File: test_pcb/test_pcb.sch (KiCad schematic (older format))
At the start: 88 parts, among them K0 KEYSW, K1 KEYSW, K10 KEYSW, K12 KEYSW, K13 KEYSW, K14 KEYSW, K15 KEYSW, K16 KEYSW, K17 KEYSW, K18 KEYSW, K2 KEYSW, K20 KEYSW, K21 KEYSW, K22 KEYSW, K3 KEYSW, K4 KEYSW, K5 KEYSW, K6 KEYSW, K7 KEYSW, K8 KEYSW, K9 KEYSW, P1 CONN_01X15, P10 CONN_01X01, P11 CONN_01X01, P12 CONN_01X01, P13 CONN_01X01, P14 CONN_01X01, P15 CONN_01X01, P2 CONN_01X08, P3 CONN_01X06, P4 CONN_01X01, P5 CONN_01X01, P6 CONN_01X01, P7 CONN_01X01, P8 CONN_01X01, P9 CONN_01X01, U1 STP16CP05

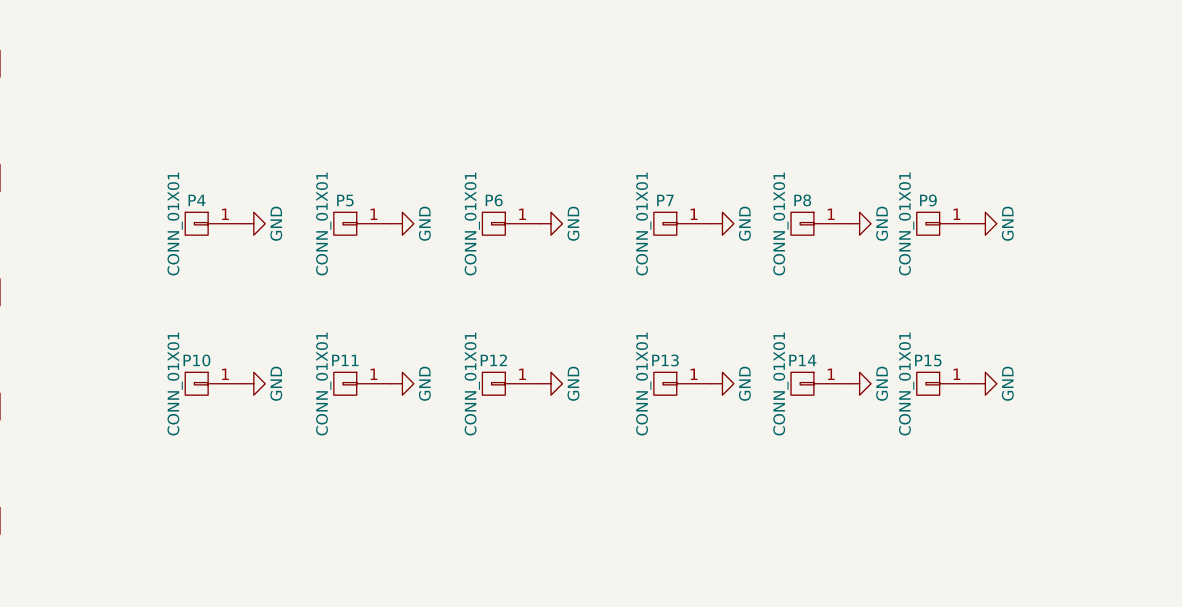
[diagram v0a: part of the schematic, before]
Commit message: test groundplane loop eliminiation, they are sneeky
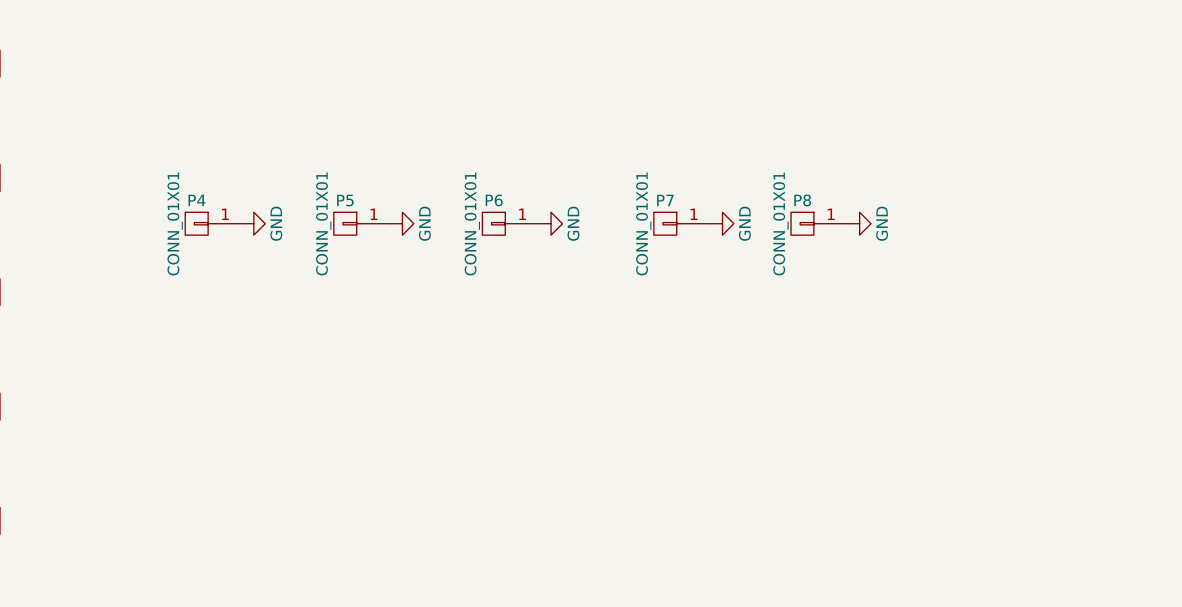
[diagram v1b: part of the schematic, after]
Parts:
- removed P10, P11, P12, P13, P14, P15, P9: CONN_01X01, Socket_Strips:Socket_Strip_Straight_1x01_Pitch1.27mm, symbol CONN_01X01
- P4, P5, P6, P7, P8: footprint Socket_Strips:Socket_Strip_Straight_1x01_Pitch1.27mm -> cherry_rgb:VIA127
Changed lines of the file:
@@
-$EndComp
-$Comp
-L GND #PWR016
-U 1 1 58BB11EE
-P 8100 5750
-F 0 "#PWR016" H 8100 5500 50  0001 C CNN
-F 1 "GND" H 8100 5600 50  0000 C CNN
-F 2 "" H 8100 5750 50  0000 C CNN
-F 3 "" H 8100 5750 50  0000 C CNN
-	1    8100 5750
-	0    -1   1    0
-$EndComp
-$Comp
-L CONN_01X01 P14
-U 1 1 58BB11E8
-P 7900 5750
-F 0 "P14" H 7900 5850 50  0000 C CNN
-F 1 "CONN_01X01" V 8000 5750 50  0000 C CNN
-F 2 "Socket_Strips:Socket_Strip_Straight_1x01_Pitch1.27mm" H 7900 5750 50  0001 C CNN
-F 3 "" H 7900 5750 50  0000 C CNN
-	1    7900 5750
-	-1   0    0    -1
-$EndComp
-$Comp
-L GND #PWR015
-U 1 1 58BB11E2
-P 8650 5750
-F 0 "#PWR015" H 8650 5500 50  0001 C CNN
-F 1 "GND" H 8650 5600 50  0000 C CNN
-F 2 "" H 8650 5750 50  0000 C CNN
-F 3 "" H 8650 5750 50  0000 C CNN
-	1    8650 5750
-	0    -1   1    0
-$EndComp
-$Comp
-L CONN_01X01 P15
-U 1 1 58BB11DC
-P 8450 5750
-F 0 "P15" H 8450 5850 50  0000 C CNN
-F 1 "CONN_01X01" V 8550 5750 50  0000 C CNN
-F 2 "Socket_Strips:Socket_Strip_Straight_1x01_Pitch1.27mm" H 8450 5750 50  0001 C CNN
-F 3 "" H 8450 5750 50  0000 C CNN
-	1    8450 5750
-	-1   0    0    -1
-$EndComp
-$Comp
-L GND #PWR014
-U 1 1 58BB11D6
-P 6750 5750
-F 0 "#PWR014" H 6750 5500 50  0001 C CNN
-F 1 "GND" H 6750 5600 50  0000 C CNN
-F 2 "" H 6750 5750 50  0000 C CNN
-F 3 "" H 6750 5750 50  0000 C CNN
-	1    6750 5750
-	0    -1   1    0
-$EndComp
-$Comp
-L CONN_01X01 P12
-U 1 1 58BB11D0
-P 6550 5750
-F 0 "P12" H 6550 5850 50  0000 C CNN
-F 1 "CONN_01X01" V 6650 5750 50  0000 C CNN
-F 2 "Socket_Strips:Socket_Strip_Straight_1x01_Pitch1.27mm" H 6550 5750 50  0001 C CNN
-F 3 "" H 6550 5750 50  0000 C CNN
-	1    6550 5750
-	-1   0    0    -1
-$EndComp
-$Comp
-L GND #PWR013
-U 1 1 58BB11CA
-P 7500 5750
-F 0 "#PWR013" H 7500 5500 50  0001 C CNN
-F 1 "GND" H 7500 5600 50  0000 C CNN
-F 2 "" H 7500 5750 50  0000 C CNN
-F 3 "" H 7500 5750 50  0000 C CNN
-	1    7500 5750
-	0    -1   1    0
-$EndComp
-$Comp
-L CONN_01X01 P13
-U 1 1 58BB11C4
-P 7300 5750
-F 0 "P13" H 7300 5850 50  0000 C CNN
-F 1 "CONN_01X01" V 7400 5750 50  0000 C CNN
-F 2 "Socket_Strips:Socket_Strip_Straight_1x01_Pitch1.27mm" H 7300 5750 50  0001 C CNN
-F 3 "" H 7300 5750 50  0000 C CNN
-	1    7300 5750
-	-1   0    0    -1
 $EndComp
 $Comp
 L GND #PWR012
-U 1 1 58BB11BE
-P 6100 5750
-F 0 "#PWR012" H 6100 5500 50  0001 C CNN
-F 1 "GND" H 6100 5600 50  0000 C CNN
-F 2 "" H 6100 5750 50  0000 C CNN
-F 3 "" H 6100 5750 50  0000 C CNN
-	1    6100 5750
-	0    -1   1    0
-$EndComp
-$Comp
-L CONN_01X01 P11
-U 1 1 58BB11B8
-P 5900 5750
-F 0 "P11" H 5900 5850 50  0000 C CNN
-F 1 "CONN_01X01" V 6000 5750 50  0000 C CNN
-F 2 "Socket_Strips:Socket_Strip_Straight_1x01_Pitch1.27mm" H 5900 5750 50  0001 C CNN
-F 3 "" H 5900 5750 50  0000 C CNN
-	1    5900 5750
-	-1   0    0    -1
-$EndComp
-$Comp
-L GND #PWR011
-U 1 1 58BB11B2
-P 5450 5750
-F 0 "#PWR011" H 5450 5500 50  0001 C CNN
-F 1 "GND" H 5450 5600 50  0000 C CNN
-F 2 "" H 5450 5750 50  0000 C CNN
-F 3 "" H 5450 5750 50  0000 C CNN
-	1    5450 5750
-	0    -1   1    0
-$EndComp
-$Comp
-L CONN_01X01 P10
-U 1 1 58BB11AC
-P 5250 5750
-F 0 "P10" H 5250 5850 50  0000 C CNN
-F 1 "CONN_01X01" V 5350 5750 50  0000 C CNN
-F 2 "Socket_Strips:Socket_Strip_Straight_1x01_Pitch1.27mm" H 5250 5750 50  0001 C CNN
-F 3 "" H 5250 5750 50  0000 C CNN
-	1    5250 5750
-	-1   0    0    -1
-$EndComp
-$Comp
-L GND #PWR010
 U 1 1 58BAEE49
 P 8100 5050
-F 0 "#PWR010" H 8100 4800 50  0001 C CNN
+F 0 "#PWR012" H 8100 4800 50  0001 C CNN
 F 1 "GND" H 8100 4900 50  0000 C CNN
 F 2 "" H 8100 5050 50  0000 C CNN
@@
 F 0 "P8" H 7900 5150 50  0000 C CNN
 F 1 "CONN_01X01" V 8000 5050 50  0000 C CNN
-F 2 "Socket_Strips:Socket_Strip_Straight_1x01_Pitch1.27mm" H 7900 5050 50  0001 C CNN
+F 2 "cherry_rgb:VIA127" H 7900 5050 50  0001 C CNN
 F 3 "" H 7900 5050 50  0000 C CNN
 	1    7900 5050
@@
 $EndComp
 $Comp
-L GND #PWR09
-U 1 1 58BAEE3D
-P 8650 5050
-F 0 "#PWR09" H 8650 4800 50  0001 C CNN
-F 1 "GND" H 8650 4900 50  0000 C CNN
-F 2 "" H 8650 5050 50  0000 C CNN
-F 3 "" H 8650 5050 50  0000 C CNN
-	1    8650 5050
-	0    -1   1    0
-$EndComp
-$Comp
-L CONN_01X01 P9
-U 1 1 58BAEE37
-P 8450 5050
-F 0 "P9" H 8450 5150 50  0000 C CNN
-F 1 "CONN_01X01" V 8550 5050 50  0000 C CNN
-F 2 "Socket_Strips:Socket_Strip_Straight_1x01_Pitch1.27mm" H 8450 5050 50  0001 C CNN
-F 3 "" H 8450 5050 50  0000 C CNN
-	1    8450 5050
-	-1   0    0    -1
-$EndComp
-$Comp
-L GND #PWR08
+L GND #PWR014
 U 1 1 58BAEE31
 P 6750 5050
-F 0 "#PWR08" H 6750 4800 50  0001 C CNN
+F 0 "#PWR014" H 6750 4800 50  0001 C CNN
 F 1 "GND" H 6750 4900 50  0000 C CNN
 F 2 "" H 6750 5050 50  0000 C CNN
@@
 F 0 "P6" H 6550 5150 50  0000 C CNN
 F 1 "CONN_01X01" V 6650 5050 50  0000 C CNN
-F 2 "Socket_Strips:Socket_Strip_Straight_1x01_Pitch1.27mm" H 6550 5050 50  0001 C CNN
+F 2 "cherry_rgb:VIA127" H 6550 5050 50  0001 C CNN
 F 3 "" H 6550 5050 50  0000 C CNN
 	1    6550 5050
@@
 $EndComp
 $Comp
-L GND #PWR07
+L GND #PWR015
 U 1 1 58BAD6B9
 P 7500 5050
-F 0 "#PWR07" H 7500 4800 50  0001 C CNN
+F 0 "#PWR015" H 7500 4800 50  0001 C CNN
 F 1 "GND" H 7500 4900 50  0000 C CNN
 F 2 "" H 7500 5050 50  0000 C CNN
@@
 F 0 "P7" H 7300 5150 50  0000 C CNN
 F 1 "CONN_01X01" V 7400 5050 50  0000 C CNN
-F 2 "Socket_Strips:Socket_Strip_Straight_1x01_Pitch1.27mm" H 7300 5050 50  0001 C CNN
+F 2 "cherry_rgb:VIA127" H 7300 5050 50  0001 C CNN
 F 3 "" H 7300 5050 50  0000 C CNN
 	1    7300 5050
@@
 $EndComp
 $Comp
-L GND #PWR06
+L GND #PWR016
 U 1 1 58BACEDF
 P 6100 5050
-F 0 "#PWR06" H 6100 4800 50  0001 C CNN
+F 0 "#PWR016" H 6100 4800 50  0001 C CNN
 F 1 "GND" H 6100 4900 50  0000 C CNN
 F 2 "" H 6100 5050 50  0000 C CNN
@@
 F 0 "P5" H 5900 5150 50  0000 C CNN
 F 1 "CONN_01X01" V 6000 5050 50  0000 C CNN
-F 2 "Socket_Strips:Socket_Strip_Straight_1x01_Pitch1.27mm" H 5900 5050 50  0001 C CNN
+F 2 "cherry_rgb:VIA127" H 5900 5050 50  0001 C CNN
 F 3 "" H 5900 5050 50  0000 C CNN
 	1    5900 5050
@@
 $EndComp
 $Comp
-L GND #PWR05
+L GND #PWR017
 U 1 1 58BABD17
 P 5450 5050
-F 0 "#PWR05" H 5450 4800 50  0001 C CNN
+F 0 "#PWR017" H 5450 4800 50  0001 C CNN
 F 1 "GND" H 5450 4900 50  0000 C CNN
 F 2 "" H 5450 5050 50  0000 C CNN
@@
 F 0 "P4" H 5250 5150 50  0000 C CNN
 F 1 "CONN_01X01" V 5350 5050 50  0000 C CNN
-F 2 "Socket_Strips:Socket_Strip_Straight_1x01_Pitch1.27mm" H 5250 5050 50  0001 C CNN
+F 2 "cherry_rgb:VIA127" H 5250 5050 50  0001 C CNN
 F 3 "" H 5250 5050 50  0000 C CNN
 	1    5250 5050

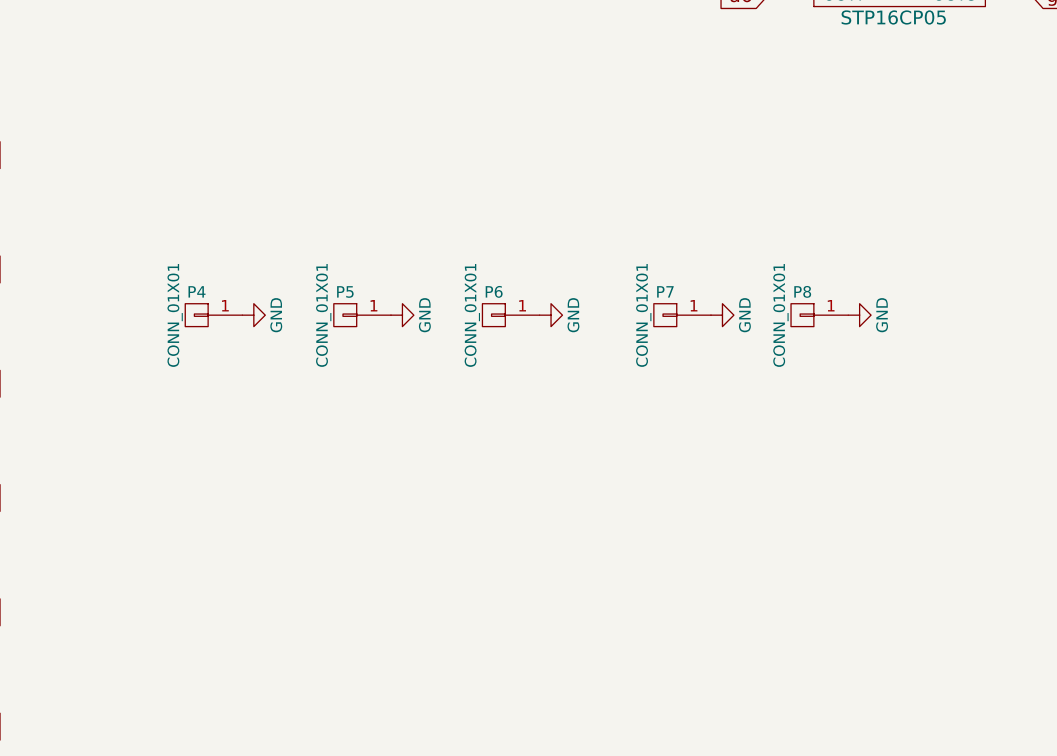
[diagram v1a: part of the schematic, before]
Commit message: test ground planes nearing completion
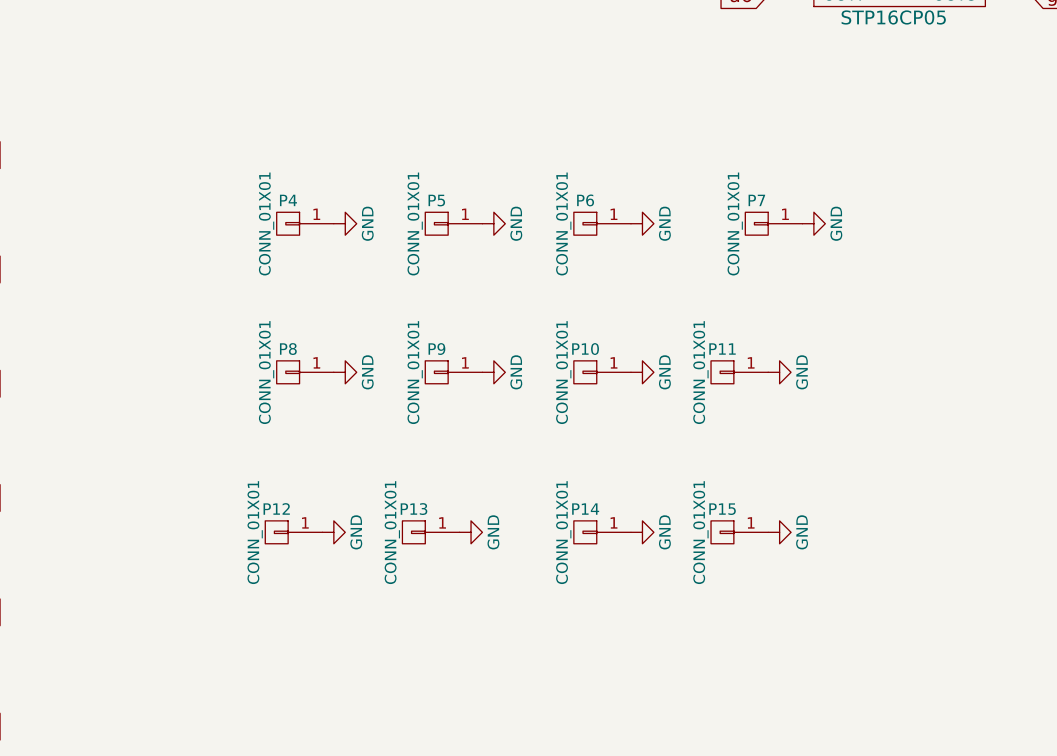
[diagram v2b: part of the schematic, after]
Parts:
- added P10, P11, P12, P13, P14, P15, P9: CONN_01X01, cherry_rgb:VIA127, symbol CONN_01X01
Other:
- moved on the sheet: P4, P5, P6, P7, P8

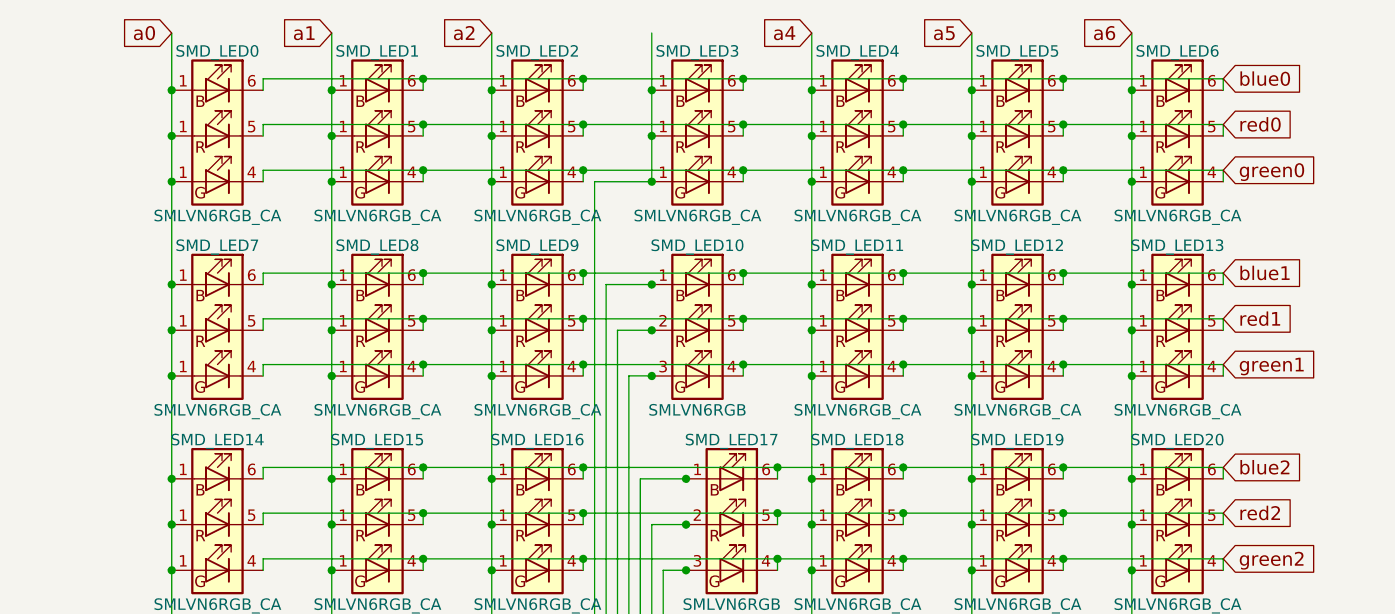
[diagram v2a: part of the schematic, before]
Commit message: renaming leds and swapping footprints
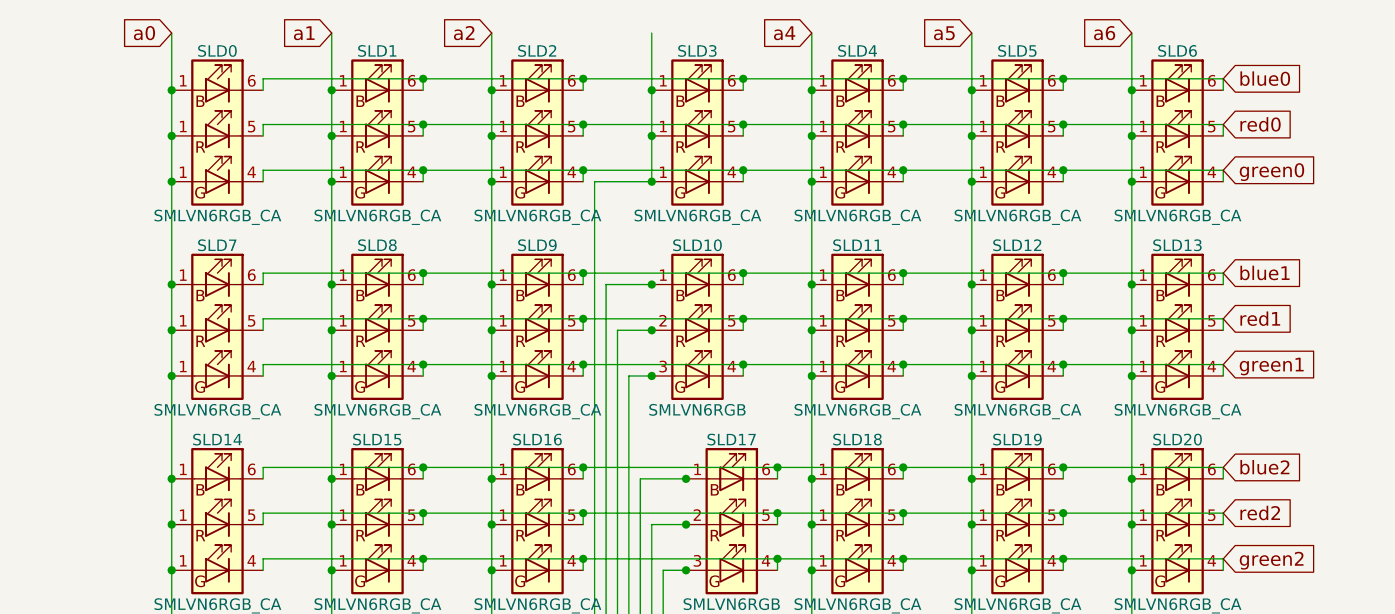
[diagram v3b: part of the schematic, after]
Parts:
- renumbered SMD_LED0 to SLD0, SMD_LED1 to SLD1, SMD_LED10 to SLD10, SMD_LED11 to SLD11, SMD_LED12 to SLD12, SMD_LED13 to SLD13, SMD_LED14 to SLD14, SMD_LED15 to SLD15, SMD_LED16 to SLD16, SMD_LED17 to SLD17, SMD_LED18 to SLD18, SMD_LED19 to SLD19, SMD_LED2 to SLD2, SMD_LED20 to SLD20, SMD_LED3 to SLD3, SMD_LED4 to SLD4, SMD_LED5 to SLD5, SMD_LED6 to SLD6, SMD_LED7 to SLD7, SMD_LED8 to SLD8, SMD_LED9 to SLD9
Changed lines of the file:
@@
 NoConn ~ -3200 7450
 $Comp
-L SMLVN6RGB_CA SMD_LED0
+L SMLVN6RGB_CA SLD0
 U 1 1 58A0BD18
 P 1000 1000
-F 0 "SMD_LED0" H 1000 1370 50  0000 C CNN
+F 0 "SLD0" H 1000 1370 50  0000 C CNN
 F 1 "SMLVN6RGB_CA" H 1000 650 50  0000 C CNN
 F 2 "cherry_rgb:SMLVN6RGB_CA" H 1000 950 50  0001 C CNN
@@
 $EndComp
 $Comp
-L SMLVN6RGB_CA SMD_LED1
+L SMLVN6RGB_CA SLD1
 U 1 1 58A0BED8
 P 1700 1000
-F 0 "SMD_LED1" H 1700 1370 50  0000 C CNN
+F 0 "SLD1" H 1700 1370 50  0000 C CNN
 F 1 "SMLVN6RGB_CA" H 1700 650 50  0000 C CNN
 F 2 "cherry_rgb:SMLVN6RGB_CA" H 1700 950 50  0001 C CNN
@@
 $EndComp
 $Comp
-L SMLVN6RGB_CA SMD_LED2
+L SMLVN6RGB_CA SLD2
 U 1 1 58A0BF71
 P 2400 1000
-F 0 "SMD_LED2" H 2400 1370 50  0000 C CNN
+F 0 "SLD2" H 2400 1370 50  0000 C CNN
 F 1 "SMLVN6RGB_CA" H 2400 650 50  0000 C CNN
 F 2 "cherry_rgb:SMLVN6RGB_CA" H 2400 950 50  0001 C CNN
@@
 $EndComp
 $Comp
-L SMLVN6RGB_CA SMD_LED3
+L SMLVN6RGB_CA SLD3
 U 1 1 58A0C01B
 P 3100 1000
-F 0 "SMD_LED3" H 3100 1370 50  0000 C CNN
+F 0 "SLD3" H 3100 1370 50  0000 C CNN
 F 1 "SMLVN6RGB_CA" H 3100 650 50  0000 C CNN
 F 2 "cherry_rgb:SMLVN6RGB_CA" H 3100 950 50  0001 C CNN
@@
 $EndComp
 $Comp
-L SMLVN6RGB_CA SMD_LED4
+L SMLVN6RGB_CA SLD4
 U 1 1 58A0E407
 P 3800 1000
-F 0 "SMD_LED4" H 3800 1370 50  0000 C CNN
+F 0 "SLD4" H 3800 1370 50  0000 C CNN
 F 1 "SMLVN6RGB_CA" H 3800 650 50  0000 C CNN
 F 2 "cherry_rgb:SMLVN6RGB_CA" H 3800 950 50  0001 C CNN
@@
 $EndComp
 $Comp
-L SMLVN6RGB_CA SMD_LED5
+L SMLVN6RGB_CA SLD5
 U 1 1 58A0E40D
 P 4500 1000
-F 0 "SMD_LED5" H 4500 1370 50  0000 C CNN
+F 0 "SLD5" H 4500 1370 50  0000 C CNN
 F 1 "SMLVN6RGB_CA" H 4500 650 50  0000 C CNN
 F 2 "cherry_rgb:SMLVN6RGB_CA" H 4500 950 50  0001 C CNN
@@
 $EndComp
 $Comp
-L SMLVN6RGB_CA SMD_LED6
+L SMLVN6RGB_CA SLD6
 U 1 1 58A0E413
 P 5200 1000
-F 0 "SMD_LED6" H 5200 1370 50  0000 C CNN
+F 0 "SLD6" H 5200 1370 50  0000 C CNN
 F 1 "SMLVN6RGB_CA" H 5200 650 50  0000 C CNN
 F 2 "cherry_rgb:SMLVN6RGB_CA" H 5200 950 50  0001 C CNN
@@
 $EndComp
 $Comp
-L SMLVN6RGB_CA SMD_LED7
+L SMLVN6RGB_CA SLD7
 U 1 1 58A100CF
 P 1000 1850
-F 0 "SMD_LED7" H 1000 2220 50  0000 C CNN
+F 0 "SLD7" H 1000 2220 50  0000 C CNN
 F 1 "SMLVN6RGB_CA" H 1000 1500 50  0000 C CNN
 F 2 "cherry_rgb:SMLVN6RGB_CA" H 1000 1800 50  0001 C CNN
@@
 $EndComp
 $Comp
-L SMLVN6RGB_CA SMD_LED8
+L SMLVN6RGB_CA SLD8
 U 1 1 58A100D5
 P 1700 1850
-F 0 "SMD_LED8" H 1700 2220 50  0000 C CNN
+F 0 "SLD8" H 1700 2220 50  0000 C CNN
 F 1 "SMLVN6RGB_CA" H 1700 1500 50  0000 C CNN
 F 2 "cherry_rgb:SMLVN6RGB_CA" H 1700 1800 50  0001 C CNN
@@
 $EndComp
 $Comp
-L SMLVN6RGB_CA SMD_LED9
+L SMLVN6RGB_CA SLD9
 U 1 1 58A100DB
 P 2400 1850
-F 0 "SMD_LED9" H 2400 2220 50  0000 C CNN
+F 0 "SLD9" H 2400 2220 50  0000 C CNN
 F 1 "SMLVN6RGB_CA" H 2400 1500 50  0000 C CNN
 F 2 "cherry_rgb:SMLVN6RGB_CA" H 2400 1800 50  0001 C CNN
@@
 $EndComp
 $Comp
-L SMLVN6RGB SMD_LED10
+L SMLVN6RGB SLD10
 U 1 1 58A100E1
 P 3100 1850
-F 0 "SMD_LED10" H 3100 2220 50  0000 C CNN
+F 0 "SLD10" H 3100 2220 50  0000 C CNN
 F 1 "SMLVN6RGB" H 3100 1500 50  0000 C CNN
 F 2 "cherry_rgb:SMLVN6RGB" H 3100 1800 50  0001 C CNN
@@
 $EndComp
 $Comp
-L SMLVN6RGB_CA SMD_LED11
+L SMLVN6RGB_CA SLD11
 U 1 1 58A100E7
 P 3800 1850
-F 0 "SMD_LED11" H 3800 2220 50  0000 C CNN
+F 0 "SLD11" H 3800 2220 50  0000 C CNN
 F 1 "SMLVN6RGB_CA" H 3800 1500 50  0000 C CNN
 F 2 "cherry_rgb:SMLVN6RGB_CA" H 3800 1800 50  0001 C CNN
@@
 $EndComp
 $Comp
-L SMLVN6RGB_CA SMD_LED12
+L SMLVN6RGB_CA SLD12
 U 1 1 58A100ED
 P 4500 1850
-F 0 "SMD_LED12" H 4500 2220 50  0000 C CNN
+F 0 "SLD12" H 4500 2220 50  0000 C CNN
 F 1 "SMLVN6RGB_CA" H 4500 1500 50  0000 C CNN
 F 2 "cherry_rgb:SMLVN6RGB_CA" H 4500 1800 50  0001 C CNN
@@
 $EndComp
 $Comp
-L SMLVN6RGB_CA SMD_LED13
+L SMLVN6RGB_CA SLD13
 U 1 1 58A100F3
 P 5200 1850
-F 0 "SMD_LED13" H 5200 2220 50  0000 C CNN
+F 0 "SLD13" H 5200 2220 50  0000 C CNN
 F 1 "SMLVN6RGB_CA" H 5200 1500 50  0000 C CNN
 F 2 "cherry_rgb:SMLVN6RGB_CA" H 5200 1800 50  0001 C CNN
@@
 $EndComp
 $Comp
-L SMLVN6RGB_CA SMD_LED14
+L SMLVN6RGB_CA SLD14
 U 1 1 58A1042B
 P 1000 2700
-F 0 "SMD_LED14" H 1000 3070 50  0000 C CNN
+F 0 "SLD14" H 1000 3070 50  0000 C CNN
 F 1 "SMLVN6RGB_CA" H 1000 2350 50  0000 C CNN
 F 2 "cherry_rgb:SMLVN6RGB_CA" H 1000 2650 50  0001 C CNN
@@
 $EndComp
 $Comp
-L SMLVN6RGB_CA SMD_LED15
+L SMLVN6RGB_CA SLD15
 U 1 1 58A10431
 P 1700 2700
-F 0 "SMD_LED15" H 1700 3070 50  0000 C CNN
+F 0 "SLD15" H 1700 3070 50  0000 C CNN
 F 1 "SMLVN6RGB_CA" H 1700 2350 50  0000 C CNN
 F 2 "cherry_rgb:SMLVN6RGB_CA" H 1700 2650 50  0001 C CNN
@@
 $EndComp
 $Comp
-L SMLVN6RGB_CA SMD_LED16
+L SMLVN6RGB_CA SLD16
 U 1 1 58A10437
 P 2400 2700
-F 0 "SMD_LED16" H 2400 3070 50  0000 C CNN
+F 0 "SLD16" H 2400 3070 50  0000 C CNN
 F 1 "SMLVN6RGB_CA" H 2400 2350 50  0000 C CNN
 F 2 "cherry_rgb:SMLVN6RGB_CA" H 2400 2650 50  0001 C CNN
@@
 $EndComp
 $Comp
-L SMLVN6RGB SMD_LED17
+L SMLVN6RGB SLD17
 U 1 1 58A1043D
 P 3250 2700
-F 0 "SMD_LED17" H 3250 3070 50  0000 C CNN
+F 0 "SLD17" H 3250 3070 50  0000 C CNN
 F 1 "SMLVN6RGB" H 3250 2350 50  0000 C CNN
 F 2 "cherry_rgb:SMLVN6RGB" H 3250 2650 50  0001 C CNN
@@
 $EndComp
 $Comp
-L SMLVN6RGB_CA SMD_LED18
+L SMLVN6RGB_CA SLD18
 U 1 1 58A10443
 P 3800 2700
-F 0 "SMD_LED18" H 3800 3070 50  0000 C CNN
+F 0 "SLD18" H 3800 3070 50  0000 C CNN
 F 1 "SMLVN6RGB_CA" H 3800 2350 50  0000 C CNN
 F 2 "cherry_rgb:SMLVN6RGB_CA" H 3800 2650 50  0001 C CNN
@@
 $EndComp
 $Comp
-L SMLVN6RGB_CA SMD_LED19
+L SMLVN6RGB_CA SLD19
 U 1 1 58A10449
 P 4500 2700
-F 0 "SMD_LED19" H 4500 3070 50  0000 C CNN
+F 0 "SLD19" H 4500 3070 50  0000 C CNN
 F 1 "SMLVN6RGB_CA" H 4500 2350 50  0000 C CNN
 F 2 "cherry_rgb:SMLVN6RGB_CA" H 4500 2650 50  0001 C CNN
@@
 $EndComp
 $Comp
-L SMLVN6RGB_CA SMD_LED20
+L SMLVN6RGB_CA SLD20
 U 1 1 58A1044F
 P 5200 2700
-F 0 "SMD_LED20" H 5200 3070 50  0000 C CNN
+F 0 "SLD20" H 5200 3070 50  0000 C CNN
 F 1 "SMLVN6RGB_CA" H 5200 2350 50  0000 C CNN
 F 2 "cherry_rgb:SMLVN6RGB_CA" H 5200 2650 50  0001 C CNN
